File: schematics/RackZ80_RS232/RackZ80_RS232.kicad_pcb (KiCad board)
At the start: 2 copper layers, 160 x 100 mm, 44 parts, among them J1 ECB_Kontron, J2 Serial 1, J3 Serial 2, Q1 BC547, SW1 Chip Select, SW2 Vector, U1 74HC245, U10 MAX232, U2 74LS02, U3 74LS32, U4 74HC245, U5 74LS138, U6 74HC245, U7 MAX232, U8 16C550, U9 16C550, X1 1.8432MHz

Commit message: Add files via upload
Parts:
- added U11: 74LS08, rackz80_footprints:DIP-14_Socket, F.Cu at (147.2, 50.7)
- moved C1 11.4 mm to (130.8, 46.2)
- moved C2 8.97 mm to (148.6, 46.2)
- moved U3 8.89 mm to (129.4, 50.7)
- moved C3 6.43 mm to (166.4, 46.2)
- moved U2 6.35 mm to (165.0, 50.7)
- moved X1 6.35 mm to (111.7, 50.7)
- moved R1 5.39 mm to (177.1, 72.3)
- moved C7 5.08 mm to (177.7, 78.0)
- moved C8 5.08 mm to (143.4, 78.0)
- moved C14 4.30 mm to (87.5, 67.9), turned to 90 degrees
- moved C13 4.26 mm to (87.5, 48.8), turned to 90 degrees
- moved C10 3.81 mm to (100.2, 46.2)
- moved U7 3.81 mm to (93.9, 50.7)
- moved C11 3.81 mm to (87.5, 53.2)
- moved C12 3.81 mm to (87.5, 59.6)
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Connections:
- J1 pad 31C: Net-(J1-Pad31C) -> /~RESET
- U1 pad 1: /~RD -> /~WR
- U1 pad 19: /~CS -> /~BUS
- U2 pad 4: Net-(U2-Pad4) -> /UART_Controller/RESET
- U2 pad 5: GND -> /~RESET
- U2 pad 6: GND -> /~RESET
- U3 pad 11: Net-(U3-Pad11) -> (no net)
- U3 pad 12: GND -> (no net)
- U3 pad 13: GND -> (no net)
- U6 pad 1: GND -> +5V
- U8 pad 35: GND -> /UART_Controller/RESET
- U9 pad 35: GND -> /UART_Controller/RESET
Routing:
- net /~RESET: track 0.00 -> 134.4 mm
- net GND: track 260.5 -> 126.7 mm
- net /UART_Controller/RESET: track 0.00 -> 89.1 mm, vias 0 -> 1
- net /~BUS: track 0.00 -> 75.2 mm, vias 0 -> 2
- net /~RD: track 174.8 -> 107.7 mm
- net /~WR: track 128.3 -> 173.4 mm
- net /~IntAck: track 42.2 -> 74.8 mm
- net +5V: track 70.7 -> 98.0 mm
- net /IntDisable: track 35.9 -> 54.9 mm
- net /CS: track 103.7 -> 114.7 mm
- net /~IORQ: track 244.3 -> 254.5 mm
- net /INT: track 38.9 -> 49.1 mm
- net /~M1: track 271.9 -> 281.7 mm
- net /UART_Controller/CLK: track 100.9 -> 109.8 mm
- net Net-(C14-Pad2): track 15.2 -> 7.40 mm
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
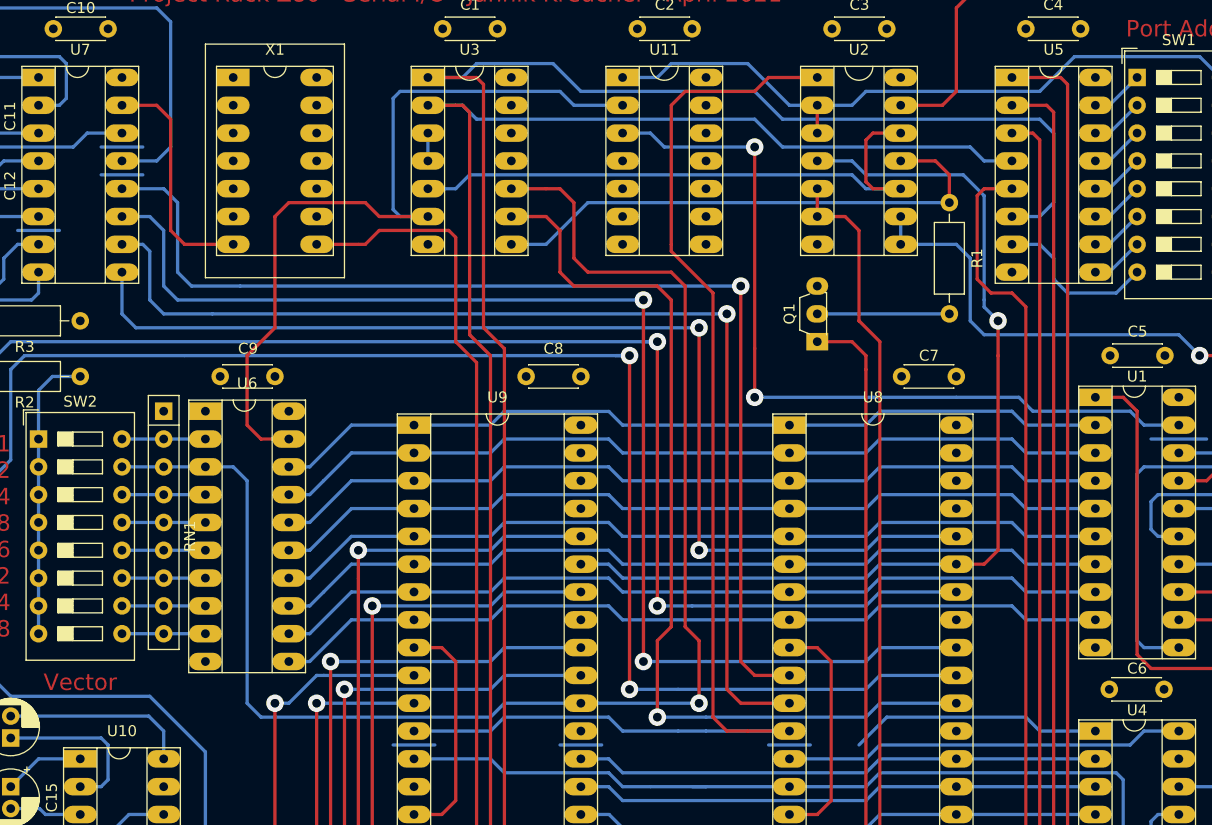
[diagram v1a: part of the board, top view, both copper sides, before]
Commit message: migrated kicad 5 to kicad 7
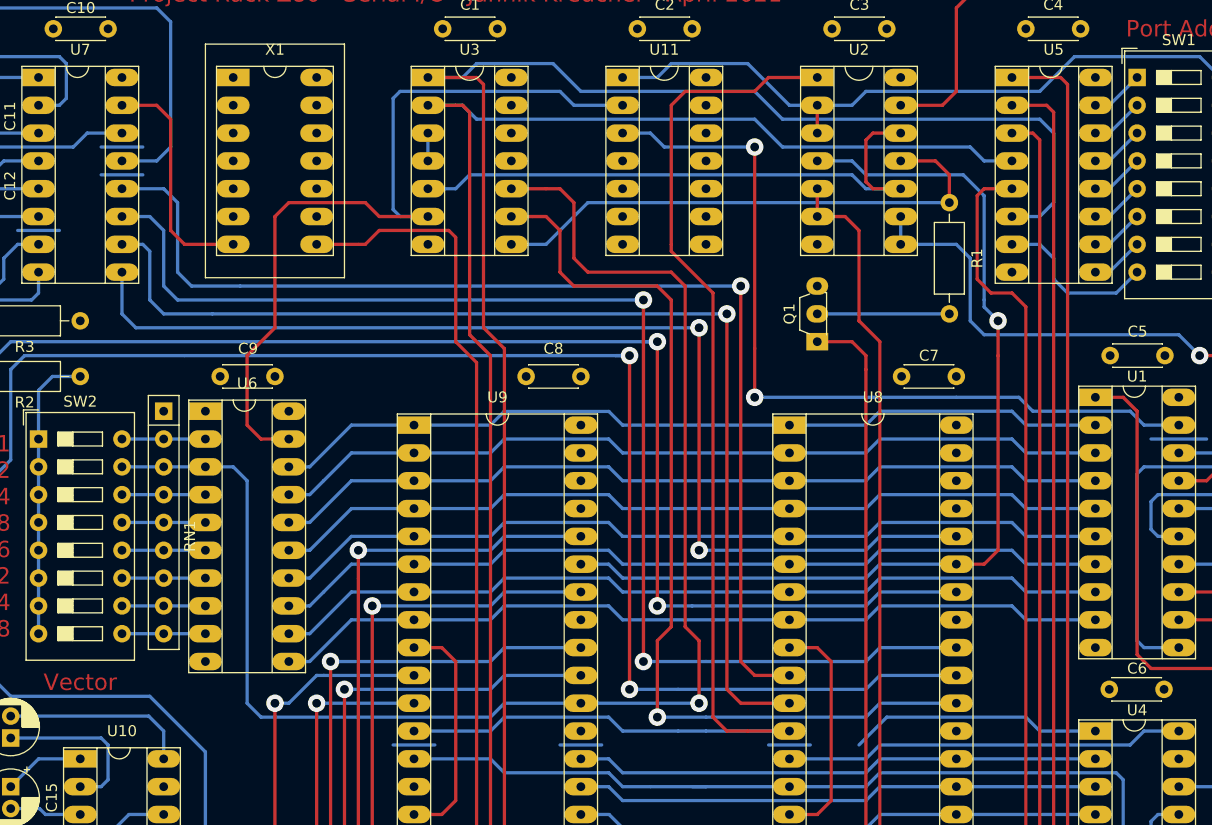
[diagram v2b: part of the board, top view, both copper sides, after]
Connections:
- net /UART_Controller/~CTS1 renamed /UART_Controller/~{CTS1}
- net /UART_Controller/~CTS2 renamed /UART_Controller/~{CTS2}
- net /UART_Controller/~LED1 renamed /UART_Controller/~{LED1}
- net /UART_Controller/~LED2 renamed /UART_Controller/~{LED2}
- net /UART_Controller/~LED3 renamed /UART_Controller/~{LED3}
- net /UART_Controller/~LED4 renamed /UART_Controller/~{LED4}
- net /UART_Controller/~RTS1 renamed /UART_Controller/~{RTS1}
- net /UART_Controller/~RTS2 renamed /UART_Controller/~{RTS2}
- net /UART_Controller/~RX1 renamed /UART_Controller/~{RX1}
- net /UART_Controller/~RX2 renamed /UART_Controller/~{RX2}
- net /UART_Controller/~TX1 renamed /UART_Controller/~{TX1}
- net /UART_Controller/~TX2 renamed /UART_Controller/~{TX2}
- net /~BUS renamed /~{BUS}
- net /~CS renamed /~{CS}
- net /~INT renamed /~{INT}
- net /~IORQ renamed /~{IORQ}
- net /~IntAck renamed /~{IntAck}
- net /~M1 renamed /~{M1}
- net /~RD renamed /~{RD}
- net /~RESET renamed /~{RESET}
- net /~WR renamed /~{WR}
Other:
- net class Default removed
